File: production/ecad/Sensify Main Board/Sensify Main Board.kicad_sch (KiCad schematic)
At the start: 9 parts

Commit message: Finished IMU, Haptics, MCU, and Root Page
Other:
- sheet Haptics ports: added GND, HAPTICS_EN; removed EN
- sheet IMU ports: added INTERRUPT1_IMU, INTERRUPT2_IMU; removed IMU_INTR1, IMU_INTR2
- sheet MCU ports: added HAPTICS_EN; removed none
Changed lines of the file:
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@@
+    (stroke (width 0) (type default))
+  )
+  (wire (pts (xy 96.52 137.16) (xy 97.79 137.16))
     (stroke (width 0) (type default))
   )
@@
     (stroke (width 0) (type default))
   )
-  (wire (pts (xy 96.52 137.16) (xy 97.79 137.16))
+  (wire (pts (xy 265.43 114.3) (xy 266.7 114.3))
+    (stroke (width 0) (type default))
+  )
+  (wire (pts (xy 96.52 132.08) (xy 97.79 132.08))
     (stroke (width 0) (type default))
   )
@@
     (stroke (width 0) (type default))
   )
-  (wire (pts (xy 96.52 132.08) (xy 97.79 132.08))
+  (wire (pts (xy 207.01 45.72) (xy 208.28 45.72))
     (stroke (width 0) (type default))
   )
@@
     (stroke (width 0) (type default))
   )
+  (wire (pts (xy 195.58 53.34) (xy 208.28 53.34))
+    (stroke (width 0) (type default))
+  )
   (wire (pts (xy 203.2 152.4) (xy 204.47 152.4))
     (stroke (width 0) (type default))
   )
   (wire (pts (xy 128.27 99.06) (xy 128.27 101.6))
+    (stroke (width 0) (type default))
+  )
+  (wire (pts (xy 207.01 68.58) (xy 208.28 68.58))
     (stroke (width 0) (type default))
   )
@@
     )
   )
+  (global_label "HAPTICS_EN" (shape output) (at 207.01 68.58 180) (fields_autoplaced)
+    (effects (font (size 1.27 1.27)) (justify right))
+    (property "Intersheetrefs" "${INTERSHEET_REFS}" (at 192.8367 68.58 0)
+      (effects (font (size 1.27 1.27)) (justify right) hide)
+    )
+  )
   (global_label "SCL" (shape input) (at 158.75 86.36 0) (fields_autoplaced)
     (effects (font (size 1.27 1.27)) (justify left))
@@
     )
   )
+  (global_label "HAPTICS_EN" (shape input) (at 266.7 114.3 0) (fields_autoplaced)
+    (effects (font (size 1.27 1.27)) (justify left))
+    (property "Intersheetrefs" "${INTERSHEET_REFS}" (at 280.8733 114.3 0)
+      (effects (font (size 1.27 1.27)) (justify left) hide)
+    )
+  )
   (global_label "SDA" (shape bidirectional) (at 203.2 152.4 180) (fields_autoplaced)
     (effects (font (size 1.27 1.27)) (justify right))
@@
     )
   )
-  (global_label "SCL" (shape input) (at 208.28 45.72 180) (fields_autoplaced)
+  (global_label "SCL" (shape input) (at 207.01 45.72 180) (fields_autoplaced)
     (effects (font (size 1.27 1.27)) (justify right))
-    (property "Intersheetrefs" "${INTERSHEET_REFS}" (at 201.7872 45.72 0)
+    (property "Intersheetrefs" "${INTERSHEET_REFS}" (at 200.5172 45.72 0)
       (effects (font (size 1.27 1.27)) (justify right) hide)
     )
@@
         (path "/9a7ba7c3-7d28-4a83-bdbc-38fbff59fcbe"
           (reference "TP1") (unit 1)
+        )
+      )
+    )
+  )
+  (symbol (lib_id "power:GND") (at 195.58 53.34 0) (unit 1)
+    (in_bom yes) (on_board yes) (dnp no) (fields_autoplaced)
+    (property "Reference" "#PWR087" (at 195.58 59.69 0)
+      (effects (font (size 1.27 1.27)) hide)
+    )
+    (property "Value" "GND" (at 195.58 58.42 0)
+      (effects (font (size 1.27 1.27)))
+    )
+    (property "Footprint" "" (at 195.58 53.34 0)
+      (effects (font (size 1.27 1.27)) hide)
+    )
+    (property "Datasheet" "" (at 195.58 53.34 0)
+      (effects (font (size 1.27 1.27)) hide)
+    )
+    (pin "1")
+    (instances
+      (project "Sensify Main Board"
+        (path "/9a7ba7c3-7d28-4a83-bdbc-38fbff59fcbe"
+          (reference "#PWR087") (unit 1)
         )
       )
@@
       (effects (font (size 1.27 1.27)) (justify left))
     )
-    (pin "EN" input (at 208.28 52.07 180)
-      (effects (font (size 1.27 1.27)) (justify left))
-    )
     (pin "SCL" input (at 208.28 45.72 180)
       (effects (font (size 1.27 1.27)) (justify left))
     )
     (pin "+5V" input (at 208.28 38.1 180)
+      (effects (font (size 1.27 1.27)) (justify left))
+    )
+    (pin "GND" input (at 208.28 53.34 180)
+      (effects (font (size 1.27 1.27)) (justify left))
+    )
+    (pin "HAPTICS_EN" output (at 208.28 68.58 180)
       (effects (font (size 1.27 1.27)) (justify left))
     )
@@
       (effects (font (size 1.27 1.27)) (justify right))
     )
-    (pin "IMU_INTR2" bidirectional (at 96.52 132.08 0)
-      (effects (font (size 1.27 1.27)) (justify right))
-    )
     (pin "SCL" input (at 96.52 142.24 0)
       (effects (font (size 1.27 1.27)) (justify right))
     )
-    (pin "IMU_INTR1" bidirectional (at 96.52 137.16 0)
-      (effects (font (size 1.27 1.27)) (justify right))
-    )
     (pin "SDA" bidirectional (at 96.52 147.32 0)
       (effects (font (size 1.27 1.27)) (justify right))
     )
     (pin "GND" bidirectional (at 96.52 152.4 0)
+      (effects (font (size 1.27 1.27)) (justify right))
+    )
+    (pin "INTERRUPT2_IMU" bidirectional (at 96.52 132.08 0)
+      (effects (font (size 1.27 1.27)) (justify right))
+    )
+    (pin "INTERRUPT1_IMU" bidirectional (at 96.52 137.16 0)
       (effects (font (size 1.27 1.27)) (justify right))
     )
@@
       (effects (font (size 1.27 1.27)) (justify left))
     )
-    (instances
+    (pin "HAPTICS_EN" input (at 265.43 114.3 0)
+      (effects (font (size 1.27 1.27)) (justify right))
+    )
+    (instances

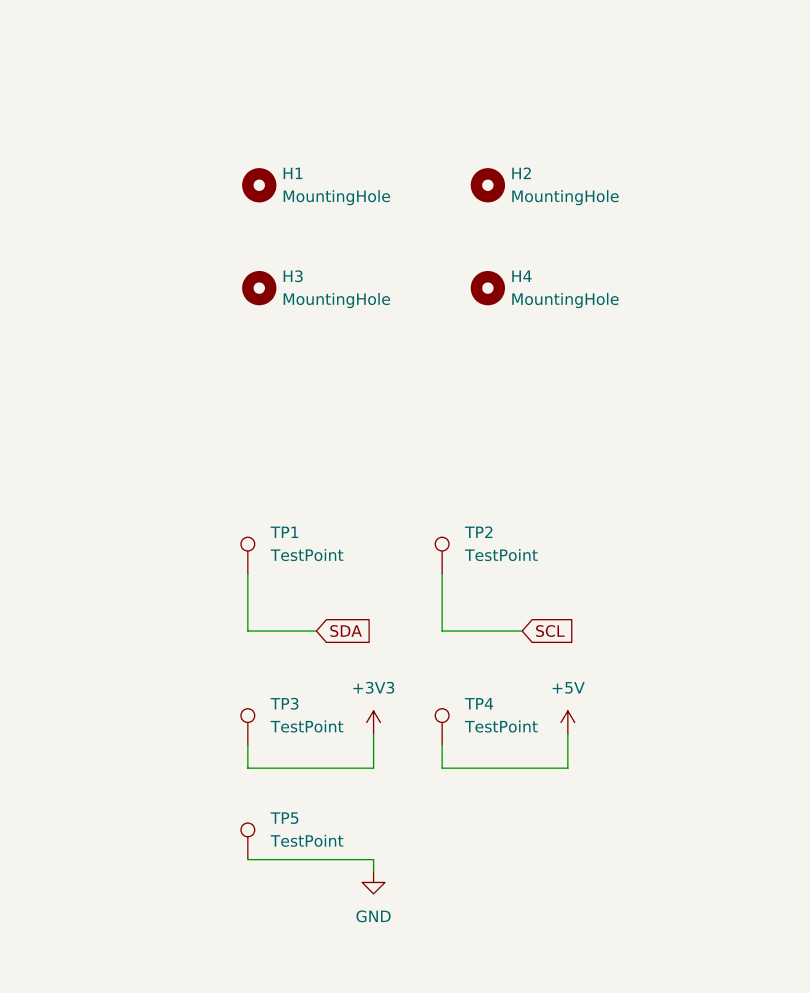
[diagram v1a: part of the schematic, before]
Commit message: Added Test Point footprints, fixed Haptics footprints, fixed IMU footprints
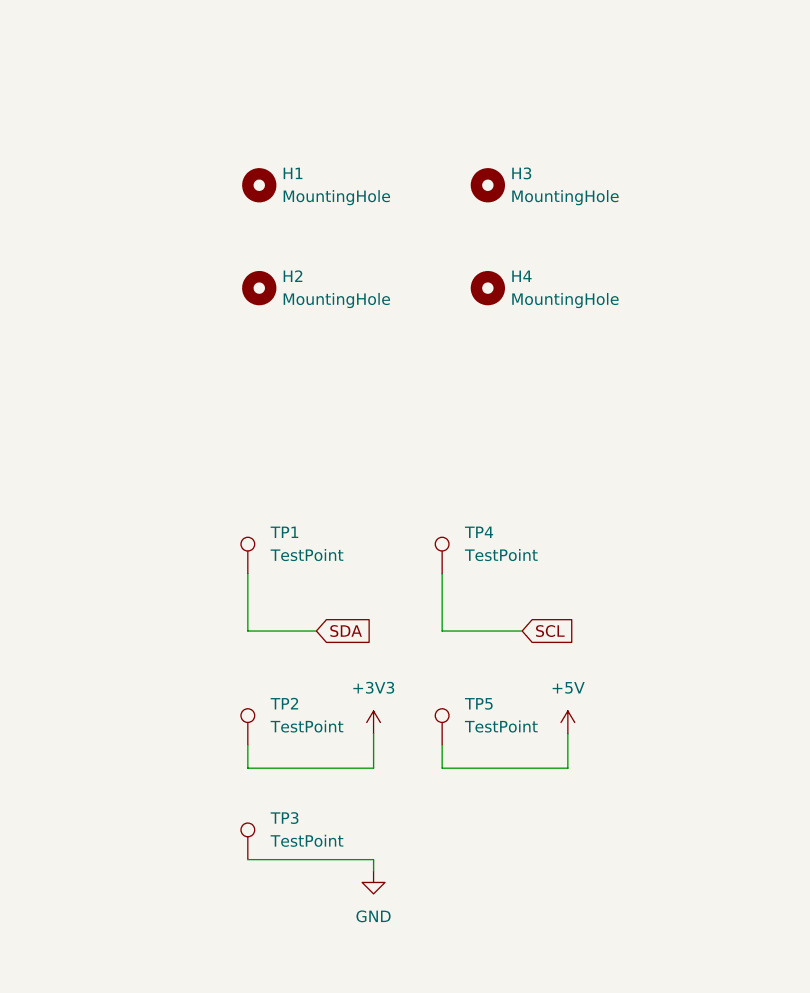
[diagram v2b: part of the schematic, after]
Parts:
- TP1: footprint (none) -> TestPoint:TestPoint_Pad_D2.0mm
- TP2: renamed from TP3; footprint (none) -> TestPoint:TestPoint_Pad_D2.0mm
- TP3: renamed from TP5; footprint (none) -> TestPoint:TestPoint_Pad_D2.0mm
- TP4: renamed from TP2; footprint (none) -> TestPoint:TestPoint_Pad_D2.0mm
- TP5: renamed from TP4; footprint (none) -> TestPoint:TestPoint_Pad_D2.0mm
- renumbered H3 to H2, H2 to H3

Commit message: Added footprints for mounting holes
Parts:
- H1, H2, H3, H4: footprint (none) -> MountingHole:MountingHole_3.2mm_M3
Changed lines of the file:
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@@
       (effects (font (size 1.27 1.27)) (justify left))
     )
-    (property "Footprint" "" (at 154.94 36.83 0)
+    (property "Footprint" "MountingHole:MountingHole_3.2mm_M3" (at 154.94 36.83 0)
       (effects (font (size 1.27 1.27)) hide)
     )
@@
       (effects (font (size 1.27 1.27)) (justify left))
     )
-    (property "Footprint" "" (at 129.54 36.83 0)
+    (property "Footprint" "MountingHole:MountingHole_3.2mm_M3" (at 129.54 36.83 0)
       (effects (font (size 1.27 1.27)) hide)
     )
@@
       (effects (font (size 1.27 1.27)) (justify left))
     )
-    (property "Footprint" "" (at 154.94 48.26 0)
+    (property "Footprint" "MountingHole:MountingHole_3.2mm_M3" (at 154.94 48.26 0)
       (effects (font (size 1.27 1.27)) hide)
     )
@@
       (effects (font (size 1.27 1.27)) (justify left))
     )
-    (property "Footprint" "" (at 129.54 48.26 0)
-      (effects (font (size 1.27 1.27)) hide)
-    )
+    (property "Footprint" "MountingHole:MountingHole_3.2mm_M3" (at 129.54 48.26 0)
+      (effects (font (size 1.27 1.27)) hide)
+    )

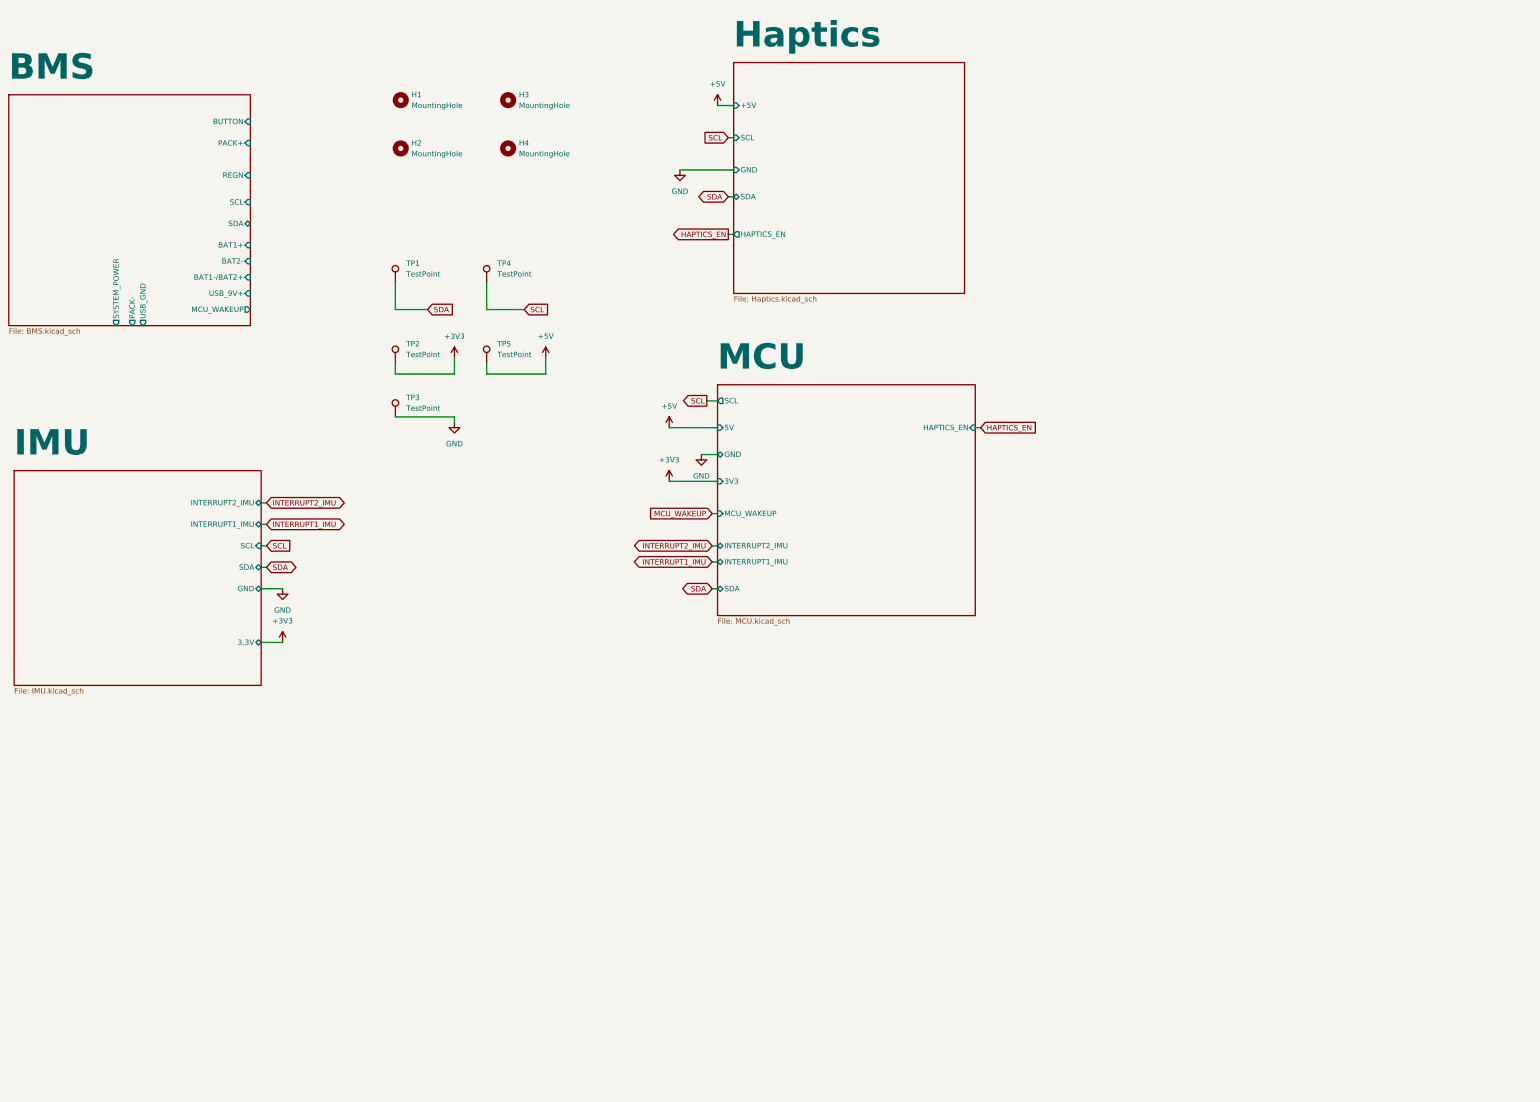
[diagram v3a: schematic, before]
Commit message: Added IO Sheet
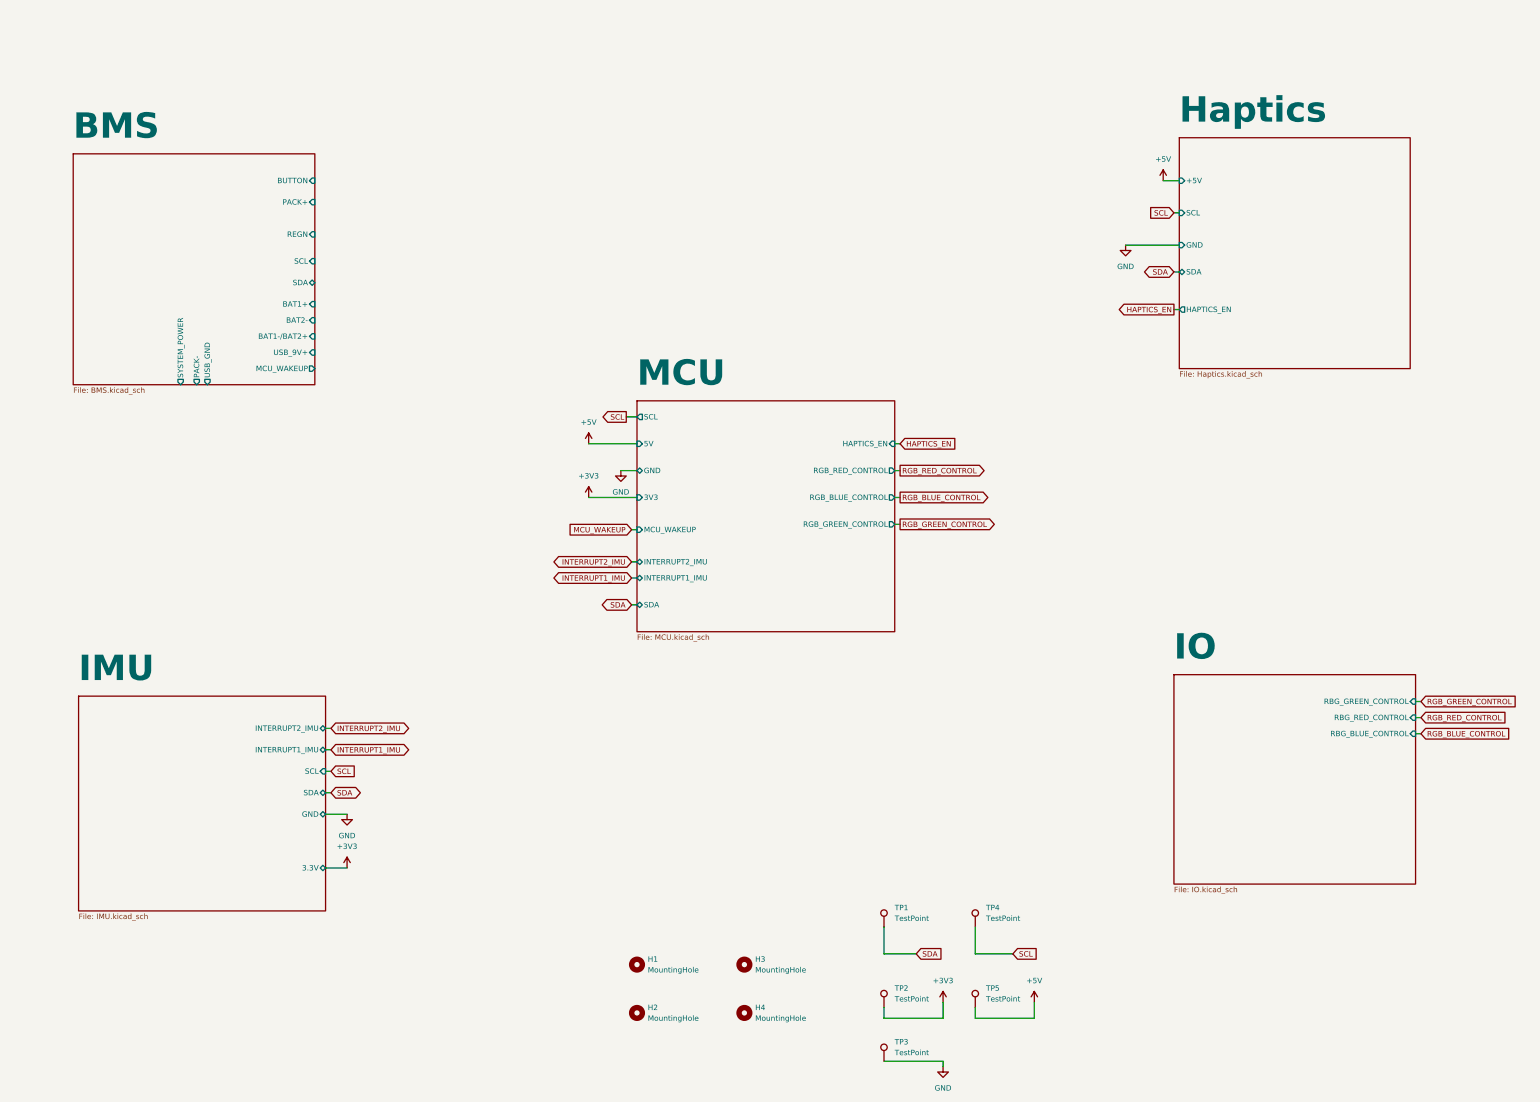
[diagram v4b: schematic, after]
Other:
- added sheet IO (IO.kicad_sch)
- sheet MCU ports: added RGB_BLUE_CONTROL, RGB_GREEN_CONTROL, RGB_RED_CONTROL; removed none
- moved on the sheet: H1, H2, H3, H4, TP1, TP2, TP3, TP4, TP5

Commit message: Deleted IO
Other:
- removed sheet IO
- sheet MCU ports: added none; removed RGB_BLUE_CONTROL, RGB_GREEN_CONTROL, RGB_RED_CONTROL
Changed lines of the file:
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@@
-    (stroke (width 0) (type default))
-  )
-  (wire (pts (xy 369.57 182.88) (xy 370.84 182.88))
-    (stroke (width 0) (type default))
-  )
-  (wire (pts (xy 246.38 137.16) (xy 247.65 137.16))
     (stroke (width 0) (type default))
   )
@@
     (stroke (width 0) (type default))
   )
-  (wire (pts (xy 369.57 186.69) (xy 370.84 186.69))
-    (stroke (width 0) (type default))
-  )
   (wire (pts (xy 184.15 149.86) (xy 185.42 149.86))
     (stroke (width 0) (type default))
   )
-  (wire (pts (xy 246.38 124.46) (xy 247.65 124.46))
-    (stroke (width 0) (type default))
-  )
   (wire (pts (xy 111.76 190.5) (xy 113.03 190.5))
     (stroke (width 0) (type default))
@@
     (stroke (width 0) (type default))
   )
-  (wire (pts (xy 246.38 130.81) (xy 247.65 130.81))
-    (stroke (width 0) (type default))
-  )
   (wire (pts (xy 173.99 130.81) (xy 185.42 130.81))
     (stroke (width 0) (type default))
@@
     (stroke (width 0) (type default))
   )
-  (wire (pts (xy 369.57 179.07) (xy 370.84 179.07))
-    (stroke (width 0) (type default))
-  )
   (wire (pts (xy 312.42 77.47) (xy 313.69 77.47))
     (stroke (width 0) (type default))
-  )
-  (global_label "RGB_RED_CONTROL" (shape output) (at 247.65 124.46 0) (fields_autoplaced)
-    (effects (font (size 1.27 1.27)) (justify left))
-    (property "Intersheetrefs" "${INTERSHEET_REFS}" (at 268.5966 124.46 0)
-      (effects (font (size 1.27 1.27)) (justify left) hide)
-    )
   )
   (global_label "INTERRUPT1_IMU" (shape bidirectional) (at 113.03 190.5 0) (fields_autoplaced)
@@
     )
   )
-  (global_label "RGB_RED_CONTROL" (shape input) (at 370.84 182.88 0) (fields_autoplaced)
-    (effects (font (size 1.27 1.27)) (justify left))
-    (property "Intersheetrefs" "${INTERSHEET_REFS}" (at 391.7866 182.88 0)
-      (effects (font (size 1.27 1.27)) (justify left) hide)
-    )
-  )
   (global_label "SCL" (shape input) (at 113.03 195.58 0) (fields_autoplaced)
     (effects (font (size 1.27 1.27)) (justify left))
@@
     )
   )
-  (global_label "RGB_BLUE_CONTROL" (shape output) (at 247.65 130.81 0) (fields_autoplaced)
-    (effects (font (size 1.27 1.27)) (justify left))
-    (property "Intersheetrefs" "${INTERSHEET_REFS}" (at 269.6852 130.81 0)
-      (effects (font (size 1.27 1.27)) (justify left) hide)
-    )
-  )
   (global_label "HAPTICS_EN" (shape input) (at 247.65 118.11 0) (fields_autoplaced)
     (effects (font (size 1.27 1.27)) (justify left))
@@
     )
   )
-  (global_label "RGB_GREEN_CONTROL" (shape output) (at 247.65 137.16 0) (fields_autoplaced)
-    (effects (font (size 1.27 1.27)) (justify left))
-    (property "Intersheetrefs" "${INTERSHEET_REFS}" (at 271.0761 137.16 0)
-      (effects (font (size 1.27 1.27)) (justify left) hide)
-    )
-  )
   (global_label "SDA" (shape bidirectional) (at 184.15 156.21 180) (fields_autoplaced)
     (effects (font (size 1.27 1.27)) (justify right))
@@
     )
   )
-  (global_label "RGB_BLUE_CONTROL" (shape input) (at 370.84 186.69 0) (fields_autoplaced)
-    (effects (font (size 1.27 1.27)) (justify left))
-    (property "Intersheetrefs" "${INTERSHEET_REFS}" (at 392.8752 186.69 0)
-      (effects (font (size 1.27 1.27)) (justify left) hide)
-    )
-  )
   (global_label "INTERRUPT1_IMU" (shape bidirectional) (at 184.15 149.86 180) (fields_autoplaced)
     (effects (font (size 1.27 1.27)) (justify right))
@@
     (property "Intersheetrefs" "${INTERSHEET_REFS}" (at 304.7554 77.47 0)
       (effects (font (size 1.27 1.27)) (justify right) hide)
-    )
-  )
-  (global_label "RGB_GREEN_CONTROL" (shape input) (at 370.84 179.07 0) (fields_autoplaced)
-    (effects (font (size 1.27 1.27)) (justify left))
-    (property "Intersheetrefs" "${INTERSHEET_REFS}" (at 394.2661 179.07 0)
-      (effects (font (size 1.27 1.27)) (justify left) hide)
     )
   )
@@
     )
   )
-  (sheet (at 312.42 172.72) (size 57.15 49.53) (fields_autoplaced)
-    (stroke (width 0.1524) (type solid))
-    (fill (color 0 0 0 0.0000))
-    (property "Sheetname" "IO" (at 312.42 169.6434 0)
-      (effects (font (size 6 6) bold) (justify left bottom))
-    )
-    (property "Sheetfile" "IO.kicad_sch" (at 312.42 222.8346 0)
-      (effects (font (size 1.27 1.27)) (justify left top))
-    )
-    (pin "RBG_GREEN_CONTROL" input (at 369.57 179.07 0)
-      (effects (font (size 1.27 1.27)) (justify right))
-    )
-    (pin "RBG_RED_CONTROL" input (at 369.57 182.88 0)
-      (effects (font (size 1.27 1.27)) (justify right))
-    )
-    (pin "RBG_BLUE_CONTROL" input (at 369.57 186.69 0)
-      (effects (font (size 1.27 1.27)) (justify right))
-    )
-    (instances
-      (project "Sensify Main Board"
-        (path "/9a7ba7c3-7d28-4a83-bdbc-38fbff59fcbe" (page "6"))
-      )
-    )
-  )
   (sheet (at 53.34 177.8) (size 58.42 50.8) (fields_autoplaced)
     (stroke (width 0.1524) (type solid))
@@
       (effects (font (size 1.27 1.27)) (justify right))
     )
-    (pin "RGB_RED_CONTROL" output (at 246.38 124.46 0)
-      (effects (font (size 1.27 1.27)) (justify right))
-    )
-    (pin "RGB_BLUE_CONTROL" output (at 246.38 130.81 0)
-      (effects (font (size 1.27 1.27)) (justify right))
-    )
-    (pin "RGB_GREEN_CONTROL" output (at 246.38 137.16 0)
-      (effects (font (size 1.27 1.27)) (justify right))
-    )
